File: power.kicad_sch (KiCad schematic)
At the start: 0 parts

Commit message: added further parts
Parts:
- added U?: TPS54202DDC, Package_TO_SOT_SMD:SOT-23-6, symbol Regulator_Switching:TPS54202DDC
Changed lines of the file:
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@@
     (effects (font (size 1.524 1.524)) (justify right))
   )
+  (symbol (lib_id "Regulator_Switching:TPS54202DDC") (at 133.35 58.42 0) (unit 1)
+    (in_bom yes) (on_board yes) (fields_autoplaced)
+    (property "Reference" "U?" (id 0) (at 133.35 48.26 0))
+    (property "Value" "TPS54202DDC" (id 1) (at 133.35 50.8 0))
+    (property "Footprint" "Package_TO_SOT_SMD:SOT-23-6" (id 2) (at 134.62 67.31 0)
+      (effects (font (size 1.27 1.27)) (justify left) hide)
+    )
+    (property "Datasheet" "http://www.ti.com/lit/ds/symlink/tps54202.pdf" (id 3) (at 125.73 49.53 0)
+      (effects (font (size 1.27 1.27)) hide)
+    )
+    (pin "1")
+    (pin "2")
+    (pin "3")
+    (pin "4")
+    (pin "5")
+    (pin "6")
+  )
 )

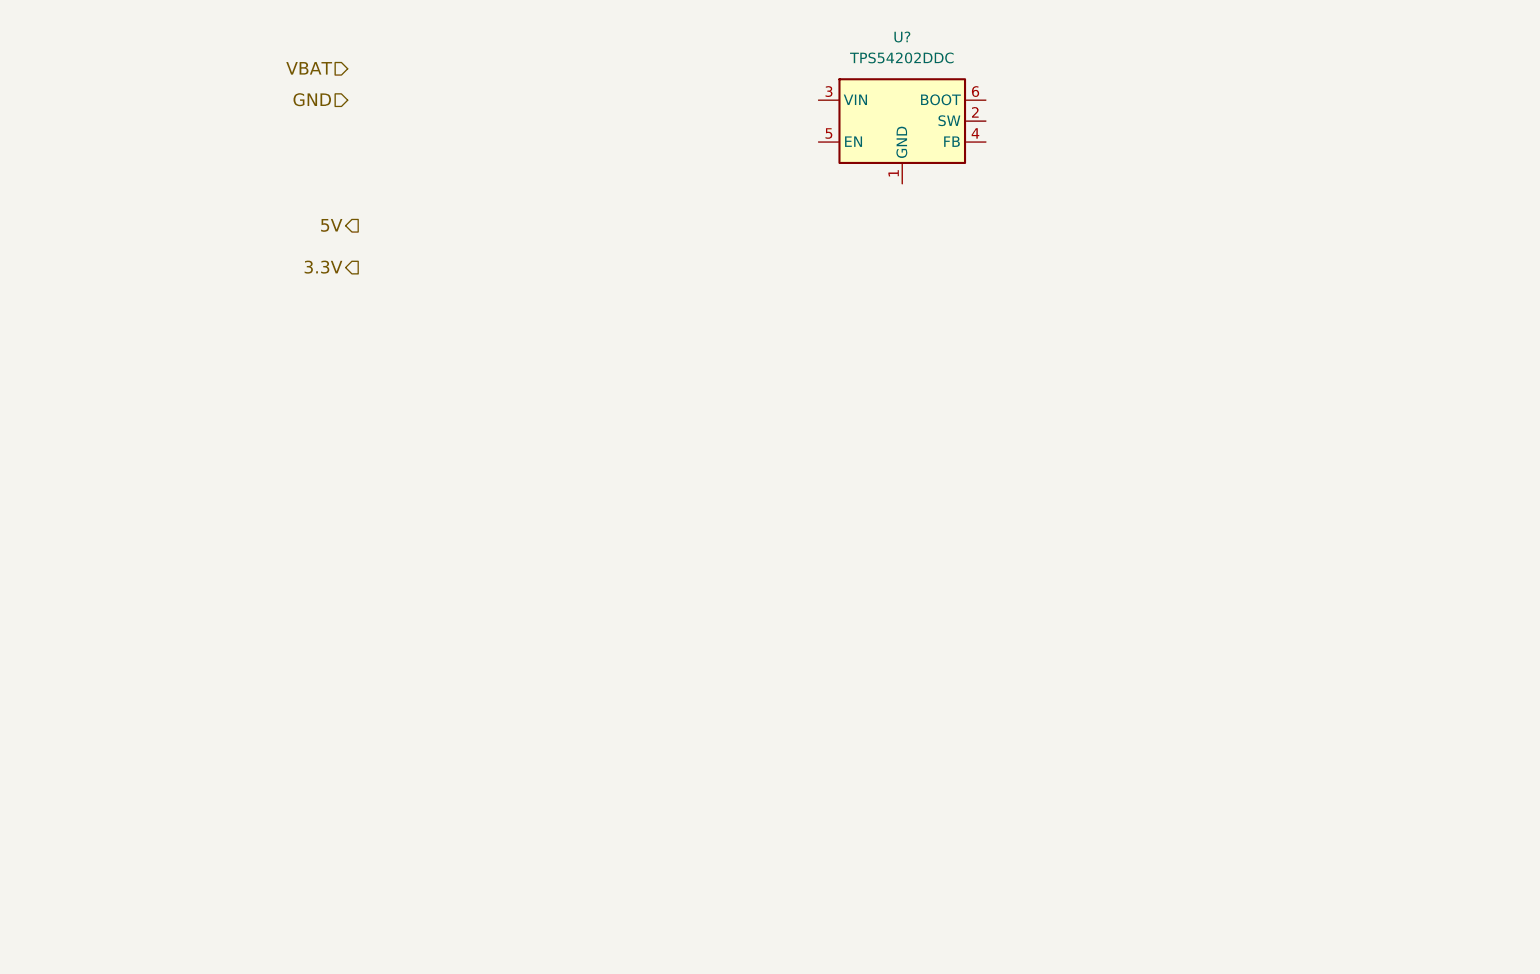
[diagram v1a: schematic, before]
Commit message: added stepUp-reg to power unit
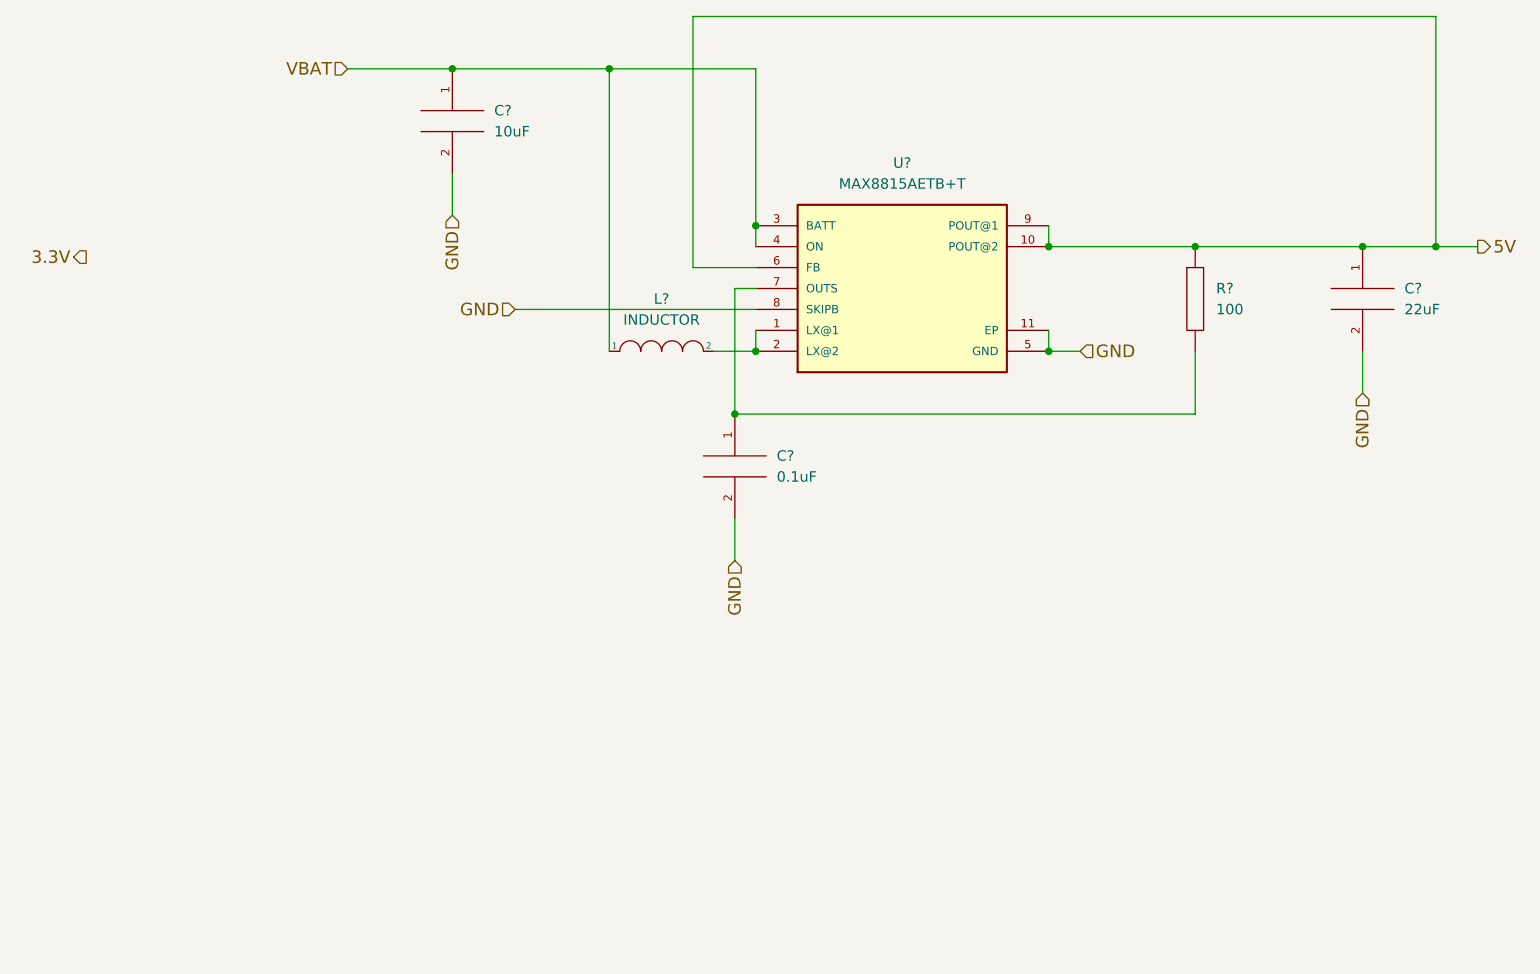
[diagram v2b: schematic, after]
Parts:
- removed U?: TPS54202DDC, Package_TO_SOT_SMD:SOT-23-6, symbol Regulator_Switching:TPS54202DDC
- added C?: 10uF, symbol pspice:C
- added C?: 0.1uF, symbol pspice:C
- added C?: 22uF, symbol pspice:C
- added L?: INDUCTOR, symbol pspice:INDUCTOR
- added R?: 100, symbol pspice:R
- added U?: MAX8815AETB+T, SON50P300X300X80-11N, symbol MAX8815AETB_T:MAX8815AETB+T
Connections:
- net 5V: now also C?.1, R?.1, U?.10 (POUT@2), U?.6 (FB), U?.9 (POUT@1)
- net GND: now also C?.2, C?.2, C?.2, U?.11 (EP), U?.5 (GND), U?.8 (SKIPB)
- net VBAT: now also C?.1, L?.1, U?.3 (BATT), U?.4 (ON)
- new net: L?.2, U?.1 (LX@1), U?.2 (LX@2)
- new net: C?.1, R?.2, U?.7 (OUTS)
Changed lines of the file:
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@@
 (kicad_sch (version 20211123) (generator eeschema)
   (paper "A4")
-  (hierarchical_label "5V" (shape output) (at 67.31 71.12 180)
-    (effects (font (size 1.524 1.524)) (justify right))
-  )
-  (hierarchical_label "3.3V" (shape output) (at 67.31 76.2 180)
-    (effects (font (size 1.524 1.524)) (justify right))
-  )
-  (hierarchical_label "GND" (shape input) (at 66.04 55.88 180)
+  (junction (at 115.57 86.36) (diameter 0) (color 0 0 0 0)
+  )
+  (junction (at 189.23 73.66) (diameter 0) (color 0 0 0 0)
+  )
+  (junction (at 113.03 93.98) (diameter 0) (color 0 0 0 0)
+  )
+  (junction (at 97.79 52.07) (diameter 0) (color 0 0 0 0)
+  )
+  (junction (at 198.12 73.66) (diameter 0) (color 0 0 0 0)
+  )
+  (junction (at 151.13 73.66) (diameter 0) (color 0 0 0 0)
+  )
+  (junction (at 78.74 52.07) (diameter 0) (color 0 0 0 0)
+  )
+  (junction (at 151.13 86.36) (diameter 0) (color 0 0 0 0)
+  )
+  (junction (at 168.91 73.66) (diameter 0) (color 0 0 0 0)
+  )
+  (junction (at 115.57 71.12) (diameter 0) (color 0 0 0 0)
+  )
+  (wire (pts (xy 107.95 76.2) (xy 107.95 45.72))
+    (stroke (width 0) (type default) (color 0 0 0 0))
+  )
+  (wire (pts (xy 189.23 86.36) (xy 189.23 91.44))
+    (stroke (width 0) (type default) (color 0 0 0 0))
+  )
+  (wire (pts (xy 151.13 71.12) (xy 151.13 73.66))
+    (stroke (width 0) (type default) (color 0 0 0 0))
+  )
+  (wire (pts (xy 115.57 83.82) (xy 115.57 86.36))
+    (stroke (width 0) (type default) (color 0 0 0 0))
+  )
+  (wire (pts (xy 115.57 76.2) (xy 107.95 76.2))
+    (stroke (width 0) (type default) (color 0 0 0 0))
+  )
+  (wire (pts (xy 168.91 73.66) (xy 189.23 73.66))
+    (stroke (width 0) (type default) (color 0 0 0 0))
+  )
+  (wire (pts (xy 97.79 52.07) (xy 115.57 52.07))
+    (stroke (width 0) (type default) (color 0 0 0 0))
+  )
+  (wire (pts (xy 86.36 81.28) (xy 115.57 81.28))
+    (stroke (width 0) (type default) (color 0 0 0 0))
+  )
+  (wire (pts (xy 113.03 78.74) (xy 115.57 78.74))
+    (stroke (width 0) (type default) (color 0 0 0 0))
+  )
+  (wire (pts (xy 198.12 45.72) (xy 198.12 73.66))
+    (stroke (width 0) (type default) (color 0 0 0 0))
+  )
+  (wire (pts (xy 113.03 106.68) (xy 113.03 111.76))
+    (stroke (width 0) (type default) (color 0 0 0 0))
+  )
+  (wire (pts (xy 78.74 52.07) (xy 97.79 52.07))
+    (stroke (width 0) (type default) (color 0 0 0 0))
+  )
+  (wire (pts (xy 151.13 73.66) (xy 168.91 73.66))
+    (stroke (width 0) (type default) (color 0 0 0 0))
+  )
+  (wire (pts (xy 198.12 73.66) (xy 203.2 73.66))
+    (stroke (width 0) (type default) (color 0 0 0 0))
+  )
+  (wire (pts (xy 107.95 45.72) (xy 198.12 45.72))
+    (stroke (width 0) (type default) (color 0 0 0 0))
+  )
+  (wire (pts (xy 110.49 86.36) (xy 115.57 86.36))
+    (stroke (width 0) (type default) (color 0 0 0 0))
+  )
+  (wire (pts (xy 113.03 93.98) (xy 113.03 78.74))
+    (stroke (width 0) (type default) (color 0 0 0 0))
+  )
+  (wire (pts (xy 115.57 52.07) (xy 115.57 71.12))
+    (stroke (width 0) (type default) (color 0 0 0 0))
+  )
+  (wire (pts (xy 151.13 86.36) (xy 154.94 86.36))
+    (stroke (width 0) (type default) (color 0 0 0 0))
+  )
+  (wire (pts (xy 189.23 73.66) (xy 198.12 73.66))
+    (stroke (width 0) (type default) (color 0 0 0 0))
+  )
+  (wire (pts (xy 78.74 64.77) (xy 78.74 69.85))
+    (stroke (width 0) (type default) (color 0 0 0 0))
+  )
+  (wire (pts (xy 66.04 52.07) (xy 78.74 52.07))
+    (stroke (width 0) (type default) (color 0 0 0 0))
+  )
+  (wire (pts (xy 97.79 52.07) (xy 97.79 86.36))
+    (stroke (width 0) (type default) (color 0 0 0 0))
+  )
+  (wire (pts (xy 168.91 93.98) (xy 113.03 93.98))
+    (stroke (width 0) (type default) (color 0 0 0 0))
+  )
+  (wire (pts (xy 115.57 71.12) (xy 115.57 73.66))
+    (stroke (width 0) (type default) (color 0 0 0 0))
+  )
+  (wire (pts (xy 168.91 86.36) (xy 168.91 93.98))
+    (stroke (width 0) (type default) (color 0 0 0 0))
+  )
+  (wire (pts (xy 151.13 83.82) (xy 151.13 86.36))
+    (stroke (width 0) (type default) (color 0 0 0 0))
+  )
+  (hierarchical_label "GND" (shape input) (at 86.36 81.28 180)
+    (effects (font (size 1.524 1.524)) (justify right))
+  )
+  (hierarchical_label "GND" (shape input) (at 78.74 69.85 270)
+    (effects (font (size 1.524 1.524)) (justify right))
+  )
+  (hierarchical_label "GND" (shape input) (at 113.03 111.76 270)
+    (effects (font (size 1.524 1.524)) (justify right))
+  )
+  (hierarchical_label "3.3V" (shape output) (at 34.29 74.93 180)
+    (effects (font (size 1.524 1.524)) (justify right))
+  )
+  (hierarchical_label "5V" (shape output) (at 203.2 73.66 0)
+    (effects (font (size 1.524 1.524)) (justify left))
+  )
+  (hierarchical_label "GND" (shape input) (at 154.94 86.36 0)
+    (effects (font (size 1.524 1.524)) (justify left))
+  )
+  (hierarchical_label "GND" (shape input) (at 189.23 91.44 270)
     (effects (font (size 1.524 1.524)) (justify right))
   )
@@
     (effects (font (size 1.524 1.524)) (justify right))
   )
-  (symbol (lib_id "Regulator_Switching:TPS54202DDC") (at 133.35 58.42 0) (unit 1)
-    (in_bom yes) (on_board yes) (fields_autoplaced)
-    (property "Reference" "U?" (id 0) (at 133.35 48.26 0))
-    (property "Value" "TPS54202DDC" (id 1) (at 133.35 50.8 0))
-    (property "Footprint" "Package_TO_SOT_SMD:SOT-23-6" (id 2) (at 134.62 67.31 0)
-      (effects (font (size 1.27 1.27)) (justify left) hide)
-    )
-    (property "Datasheet" "http://www.ti.com/lit/ds/symlink/tps54202.pdf" (id 3) (at 125.73 49.53 0)
-      (effects (font (size 1.27 1.27)) hide)
-    )
-    (pin "1")
+  (symbol (lib_id "pspice:INDUCTOR") (at 104.14 86.36 0) (unit 1)
+    (in_bom yes) (on_board yes) (fields_autoplaced)
+    (property "Reference" "L?" (id 0) (at 104.14 80.01 0))
+    (property "Value" "INDUCTOR" (id 1) (at 104.14 82.55 0))
+    (property "Footprint" "" (id 2) (at 104.14 86.36 0)
+      (effects (font (size 1.27 1.27)) hide)
+    )
+    (property "Datasheet" "~" (id 3) (at 104.14 86.36 0)
+      (effects (font (size 1.27 1.27)) hide)
+    )
+    (pin "1")
+    (pin "2")
+  )
+  (symbol (lib_id "pspice:C") (at 78.74 58.42 0) (unit 1)
+    (in_bom yes) (on_board yes) (fields_autoplaced)
+    (property "Reference" "C?" (id 0) (at 83.82 57.1499 0)
+      (effects (font (size 1.27 1.27)) (justify left))
+    )
+    (property "Value" "10uF" (id 1) (at 83.82 59.6899 0)
+      (effects (font (size 1.27 1.27)) (justify left))
+    )
+    (property "Footprint" "" (id 2) (at 78.74 58.42 0)
+      (effects (font (size 1.27 1.27)) hide)
+    )
+    (property "Datasheet" "~" (id 3) (at 78.74 58.42 0)
+      (effects (font (size 1.27 1.27)) hide)
+    )
+    (pin "1")
+    (pin "2")
+  )
+  (symbol (lib_id "pspice:C") (at 113.03 100.33 0) (unit 1)
+    (in_bom yes) (on_board yes) (fields_autoplaced)
+    (property "Reference" "C?" (id 0) (at 118.11 99.0599 0)
+      (effects (font (size 1.27 1.27)) (justify left))
+    )
+    (property "Value" "0.1uF" (id 1) (at 118.11 101.5999 0)
+      (effects (font (size 1.27 1.27)) (justify left))
+    )
+    (property "Footprint" "" (id 2) (at 113.03 100.33 0)
+      (effects (font (size 1.27 1.27)) hide)
+    )
+    (property "Datasheet" "~" (id 3) (at 113.03 100.33 0)
+      (effects (font (size 1.27 1.27)) hide)
+    )
+    (pin "1")
+    (pin "2")
+  )
+  (symbol (lib_id "pspice:C") (at 189.23 80.01 0) (unit 1)
+    (in_bom yes) (on_board yes) (fields_autoplaced)
+    (property "Reference" "C?" (id 0) (at 194.31 78.7399 0)
+      (effects (font (size 1.27 1.27)) (justify left))
+    )
+    (property "Value" "22uF" (id 1) (at 194.31 81.2799 0)
+      (effects (font (size 1.27 1.27)) (justify left))
+    )
+    (property "Footprint" "" (id 2) (at 189.23 80.01 0)
+      (effects (font (size 1.27 1.27)) hide)
+    )
+    (property "Datasheet" "~" (id 3) (at 189.23 80.01 0)
+      (effects (font (size 1.27 1.27)) hide)
+    )
+    (pin "1")
+    (pin "2")
+  )
+  (symbol (lib_id "pspice:R") (at 168.91 80.01 0) (unit 1)
+    (in_bom yes) (on_board yes) (fields_autoplaced)
+    (property "Reference" "R?" (id 0) (at 171.45 78.7399 0)
+      (effects (font (size 1.27 1.27)) (justify left))
+    )
+    (property "Value" "100" (id 1) (at 171.45 81.2799 0)
+      (effects (font (size 1.27 1.27)) (justify left))
+    )
+    (property "Footprint" "" (id 2) (at 168.91 80.01 0)
+      (effects (font (size 1.27 1.27)) hide)
+    )
+    (property "Datasheet" "~" (id 3) (at 168.91 80.01 0)
+      (effects (font (size 1.27 1.27)) hide)
+    )
+    (pin "1")
+    (pin "2")
+  )
+  (symbol (lib_id "MAX8815AETB_T:MAX8815AETB+T") (at 133.35 78.74 0) (unit 1)
+    (in_bom yes) (on_board yes) (fields_autoplaced)
+    (property "Reference" "U?" (id 0) (at 133.35 63.5 0))
+    (property "Value" "MAX8815AETB+T" (id 1) (at 133.35 66.04 0))
+    (property "Footprint" "SON50P300X300X80-11N" (id 2) (at 133.35 78.74 0)
+      (effects (font (size 1.27 1.27)) (justify bottom) hide)
+    )
+    (property "Datasheet" "" (id 3) (at 133.35 78.74 0)
+      (effects (font (size 1.27 1.27)) hide)
+    )
+    (property "MANUFACTURER" "MAXIM Semiconductor" (id 4) (at 133.35 78.74 0)
+      (effects (font (size 1.27 1.27)) (justify bottom) hide)
+    )
+    (pin "1")
+    (pin "10")
+    (pin "11")
     (pin "2")
     (pin "3")
@@
     (pin "5")
     (pin "6")
+    (pin "7")
+    (pin "8")
+    (pin "9")
   )
 )
